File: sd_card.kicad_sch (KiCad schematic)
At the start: 6 parts, among them J15 MicroSD_693071020811, U46 ESD204DQAR, U47 ESD204DQAR

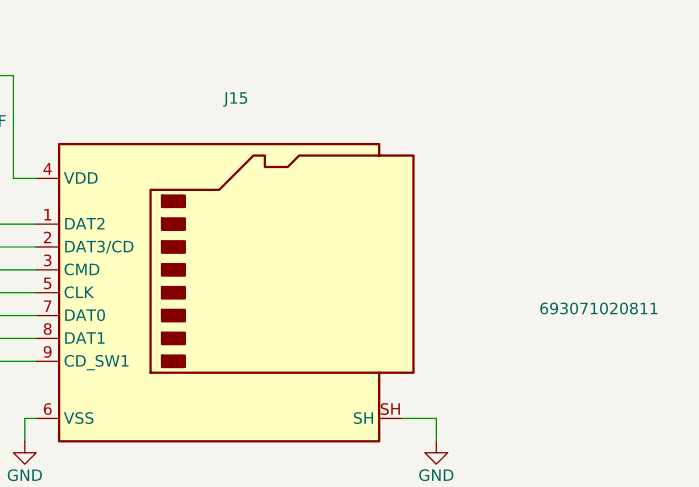
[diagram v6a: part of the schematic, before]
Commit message: [#65447] Fix rotated LEDs, overlapping text and symbols, add rules
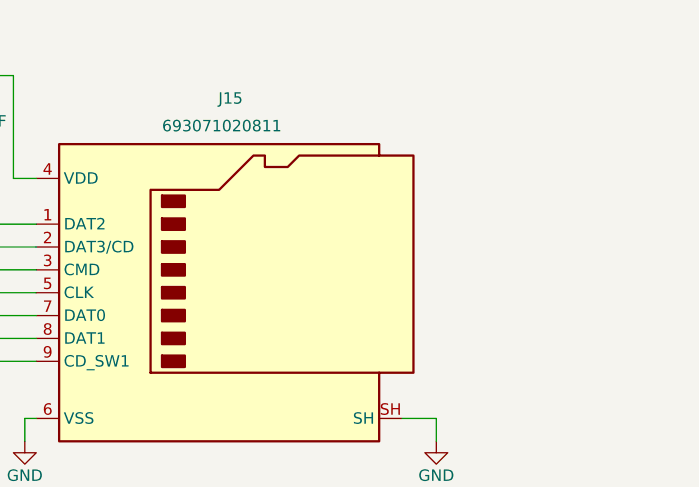
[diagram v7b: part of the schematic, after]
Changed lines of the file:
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@@
   )
   (symbol (lib_id "antmicroMemoryConnectorsPCCardSockets:MicroSD_693071020811") (at 238.76 137.16 0) (unit 1)
-    (in_bom yes) (on_board yes) (dnp no) (fields_autoplaced)
-    (property "Reference" "J15" (at 260.985 128.27 0)
+    (in_bom yes) (on_board yes) (dnp no)
+    (property "Reference" "J15" (at 260.35 128.27 0)
       (effects (font (size 1.27 1.27) (thickness 0.15)))
     )
@@
       (effects (font (size 1.27 1.27) (thickness 0.15)) (justify left bottom) hide)
     )
-    (property "MPN" "693071020811" (at 294.64 152.4 0)
+    (property "MPN" "693071020811" (at 252.73 132.08 0)
       (effects (font (size 1.27 1.27) (thickness 0.15)) (justify left bottom))
     )
